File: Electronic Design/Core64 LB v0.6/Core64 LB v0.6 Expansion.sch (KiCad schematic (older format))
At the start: 21 parts, among them J14 HEADER_11-PIN_0.1, J5 HEADER_8-PIN_0.1, J6 HEADER_8-PIN_0.1, U5 74HC238, U8 Adafruit_3.2_TFT_1743, X1 SSW-104-22-L-S-VS, X2 Header_9-PIN_0.1, X3 QWIIC, X4 SAO_conn_SFH11-NBPC-D03-ST-BK

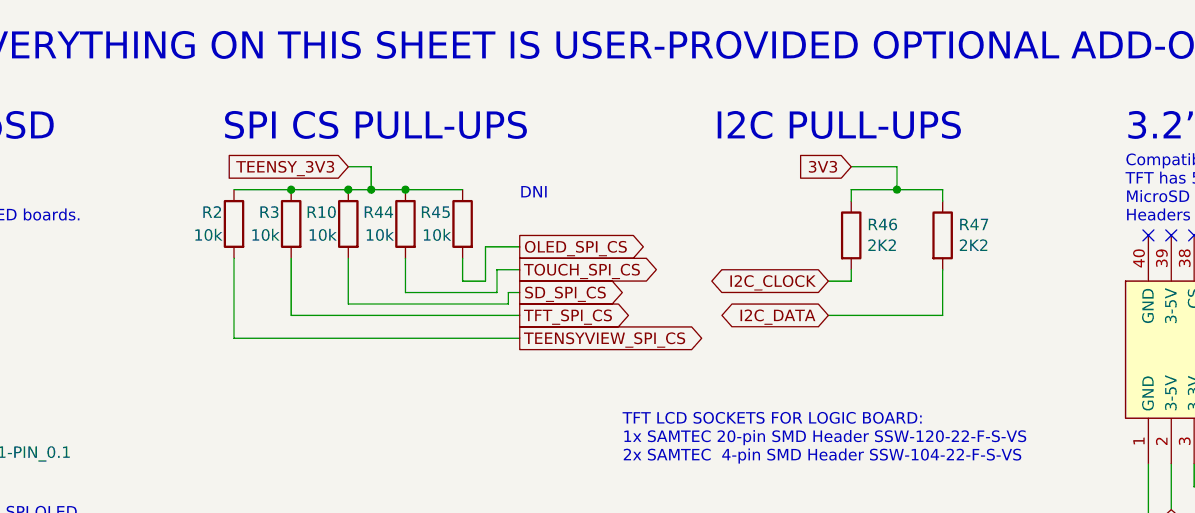
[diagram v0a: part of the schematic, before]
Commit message: APPLY LOGIC BOARD V0.5 FIXES NEEDED TO BE V0.6 U1 silk screen should be placed by pin 1 not pin 7 Check J1 and J2 labels so J1 is on the left, like it is for the Core Board Remove Header for old LED Matrix, since is no longer needed and it is in the way. RTC Notes on schematic, must add THREE things, typo change from TWO. Below JP5 Teensy Charge Enable is a rogue "+" on the silk screen Left of R56 is a dead-end trace stub. Doesn't hurt anything but it's not right. 6.8 Ohm Core Current Limit Resistors can move to 5%. JP1/2 for OLED should be JP1/2 on the OLED silk screen, not JP3/4 Silk screen, left header row, swap SEN1 and SEN2 text so they match to S1 and S2 correctly on the inner perimeter. Move to larger logo and other text on the backside Update silk screen for all boards with P/Ns, bare board. Move top row of TFT LCD support down 0.55mm. Add 470 resistor to gate of core array enable to limit current. Change I2C pull-up resistors from 2.2K to 1.2K 20% (E12 series is most common, and values overlap) Remove two dead-end GND (BAT-) traces between/below Teensy 25/26, and over to QWIIC. Add I2C series resistors 68 Ohm at output of Teensy. Move the 470uF LED 5V0 capacitor, down to be between 5V0 Cur Mon and Teensy Charge enable jumpers, out of the way of the batteries. New stylus position is on left, so the 3V3 capacitor needs to move in a few mm to allow it to pass through. Provide thru-holes for alternate 3.3V and 5V bulk capacitor options. Propagation through sense logic chips was 200ns, reduce PU to 1K2 and remove inline 10Ks. Now 50ns. Voltage divider and other resistors, consolidated to 10K resistors. Keep the two 10K resistors on the 5V0 MON. Add a SJ in series to isolate from Hall Switches. Replace the inline 10K resistors in the all optional Voltage Monitoring lines with closed SJs instead. Clean-up all the horz/vert traces left from removing LED drive header and relocating the driver and 5V0 cap Part substitutions Data sheet updates
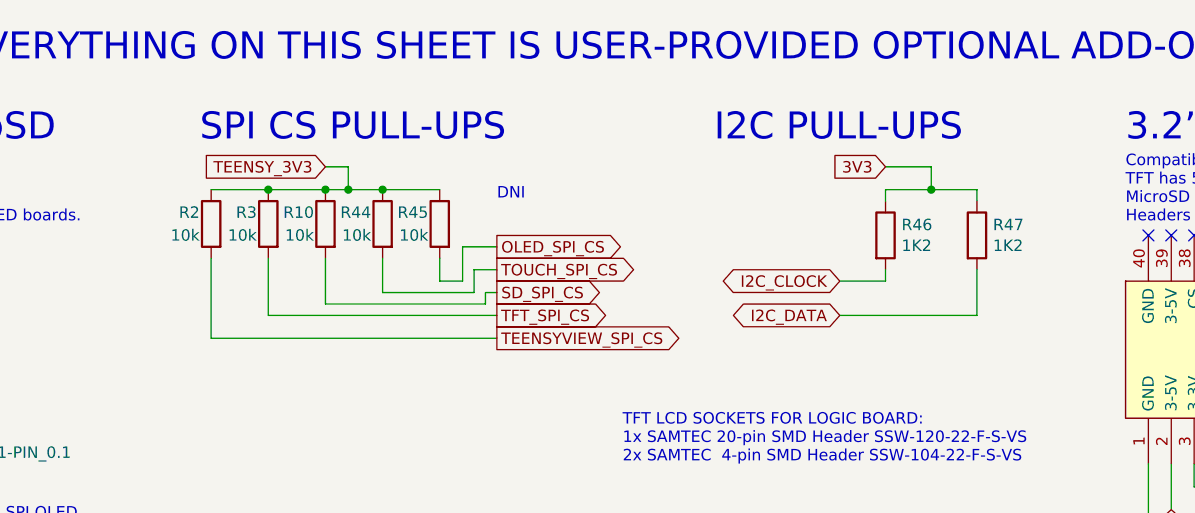
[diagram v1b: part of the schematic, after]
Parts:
- R46, R47: value 2K2 -> 1K2
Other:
- moved on the sheet: R10, R2, R3, R44, R45, R46, R47
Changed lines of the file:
@@
 L Device:R R?
 U 1 1 5FAF4975
-P 6350 1400
+P 6500 1400
 AR Path="/5E755787/5FAF4975" Ref="R?"  Part="1"
 AR Path="/5E755AC8/5D2551FF/5FAF4975" Ref="R?"  Part="1"
 AR Path="/5FAF4975" Ref="R?"  Part="1"
 AR Path="/5EA63449/5FAF4975" Ref="R46"  Part="1"
-F 0 "R46" H 6420 1446 50  0000 L CNN
-F 1 "2K2" H 6420 1355 50  0000 L CNN
-F 2 "Resistor_SMD:R_0805_2012Metric" V 6280 1400 50  0001 C CNN
-F 3 "~" H 6350 1400 50  0001 C CNN
-	1    6350 1400
+F 0 "R46" H 6570 1446 50  0000 L CNN
+F 1 "1K2" H 6570 1355 50  0000 L CNN
+F 2 "Resistor_SMD:R_0805_2012Metric" V 6430 1400 50  0001 C CNN
+F 3 "~" H 6500 1400 50  0001 C CNN
+	1    6500 1400
 	1    0    0    -1
 $EndComp
@@
 L Device:R R?
 U 1 1 5FAF497B
-P 6750 1400
+P 6900 1400
 AR Path="/5E755787/5FAF497B" Ref="R?"  Part="1"
 AR Path="/5E755AC8/5D2551FF/5FAF497B" Ref="R?"  Part="1"
 AR Path="/5FAF497B" Ref="R?"  Part="1"
 AR Path="/5EA63449/5FAF497B" Ref="R47"  Part="1"
-F 0 "R47" H 6820 1446 50  0000 L CNN
-F 1 "2K2" H 6820 1355 50  0000 L CNN
-F 2 "Resistor_SMD:R_0805_2012Metric" V 6680 1400 50  0001 C CNN
-F 3 "~" H 6750 1400 50  0001 C CNN
-	1    6750 1400
-	1    0    0    -1
-$EndComp
-Wire Wire Line
-	6250 1600 6350 1600
-Wire Wire Line
-	6350 1550 6350 1600
-Text GLabel 6250 1750 0    50   BiDi ~ 0
+F 0 "R47" H 6970 1446 50  0000 L CNN
+F 1 "1K2" H 6970 1355 50  0000 L CNN
+F 2 "Resistor_SMD:R_0805_2012Metric" V 6830 1400 50  0001 C CNN
+F 3 "~" H 6900 1400 50  0001 C CNN
+	1    6900 1400
+	1    0    0    -1
+$EndComp
+Wire Wire Line
+	6500 1550 6500 1600
+Text GLabel 6300 1750 0    50   BiDi ~ 0
 I2C_DATA
-Text GLabel 6250 1600 0    50   BiDi ~ 0
+Text GLabel 6300 1600 0    50   BiDi ~ 0
 I2C_CLOCK
 Text Notes 5750 1000 0    118  ~ 0
 I2C PULL-UPS
-Text GLabel 6350 1100 0    50   Input ~ 0
+Text GLabel 6500 1100 0    50   Input ~ 0
 3V3
 Wire Wire Line
-	6750 1200 6750 1250
-Wire Wire Line
-	6550 1100 6350 1100
-Wire Wire Line
-	6350 1200 6350 1250
-Wire Wire Line
-	6350 1200 6550 1200
-Connection ~ 6550 1200
-Wire Wire Line
-	6550 1200 6750 1200
+	6900 1200 6900 1250
+Wire Wire Line
+	6700 1100 6500 1100
+Wire Wire Line
+	6500 1200 6500 1250
+Wire Wire Line
+	6500 1200 6700 1200
+Connection ~ 6700 1200
+Wire Wire Line
+	6700 1200 6900 1200
 $Comp
 L Device:R R?
 U 1 1 5FB255AB
-P 3900 1350
+P 3800 1350
 AR Path="/5E755787/5FB255AB" Ref="R?"  Part="1"
 AR Path="/5E755AC8/5D2551FF/5FB255AB" Ref="R?"  Part="1"
 AR Path="/5FB255AB" Ref="R?"  Part="1"
 AR Path="/5EA63449/5FB255AB" Ref="R3"  Part="1"
-F 0 "R3" H 3950 1400 50  0000 L CNN
-F 1 "10k" H 3950 1300 50  0000 L CNN
-F 2 "Resistor_SMD:R_0805_2012Metric" V 3830 1350 50  0001 C CNN
-F 3 "~" H 3900 1350 50  0001 C CNN
-	1    3900 1350
-	-1   0    0    -1
-$EndComp
-Text GLabel 4900 1750 2    50   Output ~ 0
+F 0 "R3" H 3850 1400 50  0000 L CNN
+F 1 "10k" H 3850 1300 50  0000 L CNN
+F 2 "Resistor_SMD:R_0805_2012Metric" V 3730 1350 50  0001 C CNN
+F 3 "~" H 3800 1350 50  0001 C CNN
+	1    3800 1350
+	-1   0    0    -1
+$EndComp
+Text GLabel 4800 1750 2    50   Output ~ 0
 TFT_SPI_CS
-Text GLabel 4900 1550 2    50   Output ~ 0
+Text GLabel 4800 1550 2    50   Output ~ 0
 TOUCH_SPI_CS
-Text GLabel 4900 1450 2    50   Output ~ 0
+Text GLabel 4800 1450 2    50   Output ~ 0
 OLED_SPI_CS
-Text GLabel 4900 1650 2    50   Output ~ 0
+Text GLabel 4800 1650 2    50   Output ~ 0
 SD_SPI_CS
-Text GLabel 4900 1850 2    50   Output ~ 0
+Text GLabel 4800 1850 2    50   Output ~ 0
 TEENSYVIEW_SPI_CS
 $Comp
 L Device:R R?
 U 1 1 5FB255B6
-P 4150 1350
+P 4050 1350
 AR Path="/5E755787/5FB255B6" Ref="R?"  Part="1"
 AR Path="/5E755AC8/5D2551FF/5FB255B6" Ref="R?"  Part="1"
 AR Path="/5FB255B6" Ref="R?"  Part="1"
 AR Path="/5EA63449/5FB255B6" Ref="R10"  Part="1"
-F 0 "R10" H 4200 1400 50  0000 L CNN
-F 1 "10k" H 4200 1300 50  0000 L CNN
-F 2 "Resistor_SMD:R_0805_2012Metric" V 4080 1350 50  0001 C CNN
-F 3 "~" H 4150 1350 50  0001 C CNN
-	1    4150 1350
+F 0 "R10" H 4100 1400 50  0000 L CNN
+F 1 "10k" H 4100 1300 50  0000 L CNN
+F 2 "Resistor_SMD:R_0805_2012Metric" V 3980 1350 50  0001 C CNN
+F 3 "~" H 4050 1350 50  0001 C CNN
+	1    4050 1350
 	-1   0    0    -1
 $EndComp
@@
 L Device:R R?
 U 1 1 5FB255BC
-P 4400 1350
+P 4300 1350
 AR Path="/5E755787/5FB255BC" Ref="R?"  Part="1"
 AR Path="/5E755AC8/5D2551FF/5FB255BC" Ref="R?"  Part="1"
 AR Path="/5FB255BC" Ref="R?"  Part="1"
 AR Path="/5EA63449/5FB255BC" Ref="R44"  Part="1"
-F 0 "R44" H 4450 1400 50  0000 L CNN
-F 1 "10k" H 4450 1300 50  0000 L CNN
-F 2 "Resistor_SMD:R_0805_2012Metric" V 4330 1350 50  0001 C CNN
-F 3 "~" H 4400 1350 50  0001 C CNN
-	1    4400 1350
+F 0 "R44" H 4350 1400 50  0000 L CNN
+F 1 "10k" H 4350 1300 50  0000 L CNN
+F 2 "Resistor_SMD:R_0805_2012Metric" V 4230 1350 50  0001 C CNN
+F 3 "~" H 4300 1350 50  0001 C CNN
+	1    4300 1350
 	-1   0    0    -1
 $EndComp
@@
 L Device:R R?
 U 1 1 5FB255C2
-P 4650 1350
+P 4550 1350
 AR Path="/5E755787/5FB255C2" Ref="R?"  Part="1"
 AR Path="/5E755AC8/5D2551FF/5FB255C2" Ref="R?"  Part="1"
 AR Path="/5FB255C2" Ref="R?"  Part="1"
 AR Path="/5EA63449/5FB255C2" Ref="R45"  Part="1"
-F 0 "R45" H 4700 1400 50  0000 L CNN
-F 1 "10k" H 4700 1300 50  0000 L CNN
-F 2 "Resistor_SMD:R_0805_2012Metric" V 4580 1350 50  0001 C CNN
-F 3 "~" H 4650 1350 50  0001 C CNN
-	1    4650 1350
+F 0 "R45" H 4600 1400 50  0000 L CNN
+F 1 "10k" H 4600 1300 50  0000 L CNN
+F 2 "Resistor_SMD:R_0805_2012Metric" V 4480 1350 50  0001 C CNN
+F 3 "~" H 4550 1350 50  0001 C CNN
+	1    4550 1350
 	-1   0    0    -1
 $EndComp
@@
 L Device:R R?
 U 1 1 5FB255C8
-P 3650 1350
+P 3550 1350
 AR Path="/5E755787/5FB255C8" Ref="R?"  Part="1"
 AR Path="/5E755AC8/5D2551FF/5FB255C8" Ref="R?"  Part="1"
 AR Path="/5FB255C8" Ref="R?"  Part="1"
 AR Path="/5EA63449/5FB255C8" Ref="R2"  Part="1"
-F 0 "R2" H 3700 1400 50  0000 L CNN
-F 1 "10k" H 3700 1300 50  0000 L CNN
-F 2 "Resistor_SMD:R_0805_2012Metric" V 3580 1350 50  0001 C CNN
-F 3 "~" H 3650 1350 50  0001 C CNN
-	1    3650 1350
-	-1   0    0    -1
-$EndComp
-Wire Wire Line
-	4900 1450 4750 1450
-Wire Wire Line
-	4750 1450 4750 1600
-Wire Wire Line
-	4750 1600 4650 1600
-Wire Wire Line
-	4650 1600 4650 1500
-Wire Wire Line
-	4900 1550 4800 1550
-Wire Wire Line
-	4800 1550 4800 1650
-Wire Wire Line
-	4800 1650 4400 1650
-Wire Wire Line
-	4400 1650 4400 1500
-Wire Wire Line
-	4900 1650 4850 1650
-Wire Wire Line
-	4850 1650 4850 1700
-Wire Wire Line
-	4850 1700 4150 1700
-Wire Wire Line
-	4150 1700 4150 1500
-Wire Wire Line
-	4900 1750 3900 1750
-Wire Wire Line
-	3900 1750 3900 1500
-Wire Wire Line
-	4900 1850 3650 1850
-Wire Wire Line
-	3650 1850 3650 1500
-Connection ~ 3900 1200
-Wire Wire Line
-	3900 1200 3650 1200
+F 0 "R2" H 3600 1400 50  0000 L CNN
+F 1 "10k" H 3600 1300 50  0000 L CNN
+F 2 "Resistor_SMD:R_0805_2012Metric" V 3480 1350 50  0001 C CNN
+F 3 "~" H 3550 1350 50  0001 C CNN
+	1    3550 1350
+	-1   0    0    -1
+$EndComp
+Wire Wire Line
+	4800 1450 4650 1450
+Wire Wire Line
+	4650 1450 4650 1600
+Wire Wire Line
+	4650 1600 4550 1600
+Wire Wire Line
+	4550 1600 4550 1500
+Wire Wire Line
+	4800 1550 4700 1550
+Wire Wire Line
+	4700 1550 4700 1650
+Wire Wire Line
+	4700 1650 4300 1650
+Wire Wire Line
+	4300 1650 4300 1500
+Wire Wire Line
+	4800 1650 4750 1650
+Wire Wire Line
+	4750 1650 4750 1700
+Wire Wire Line
+	4750 1700 4050 1700
+Wire Wire Line
+	4050 1700 4050 1500
+Wire Wire Line
+	4800 1750 3800 1750
+Wire Wire Line
+	3800 1750 3800 1500
+Wire Wire Line
+	4800 1850 3550 1850
+Wire Wire Line
+	3550 1850 3550 1500
+Connection ~ 3800 1200
+Wire Wire Line
+	3800 1200 3550 1200
+Connection ~ 4050 1200
+Wire Wire Line
+	4050 1200 4150 1200
+Connection ~ 4300 1200
+Wire Wire Line
+	4300 1200 4150 1200
+Wire Wire Line
+	4550 1200 4300 1200
+Wire Wire Line
+	4050 1100 4150 1100
 Connection ~ 4150 1200
 Wire Wire Line
-	4150 1200 4250 1200
-Connection ~ 4400 1200
-Wire Wire Line
-	4400 1200 4250 1200
-Wire Wire Line
-	4650 1200 4400 1200
-Wire Wire Line
-	4150 1100 4250 1100
-Connection ~ 4250 1200
-Wire Wire Line
-	4150 1200 3900 1200
-Wire Wire Line
-	4250 1100 4250 1200
-Text Notes 3600 1000 0    118  ~ 0
+	4050 1200 3800 1200
+Wire Wire Line
+	4150 1100 4150 1200
+Text Notes 3500 1000 0    118  ~ 0
 SPI CS PULL-UPS
 Wire Wire Line
-	6550 1100 6550 1200
-Wire Wire Line
-	6750 1550 6750 1750
-Wire Wire Line
-	6750 1750 6250 1750
-Text Notes 4900 1250 0    50   ~ 0
+	6700 1100 6700 1200
+Wire Wire Line
+	6900 1550 6900 1750
+Text Notes 4800 1250 0    50   ~ 0
 DNI
 Text GLabel 6850 3700 0    50   Output ~ 0
@@
 Text Notes 9450 4750 0    59   ~ 0
 CARD DETECT\nDAT2\nD1\nCS (or D3)\nSI (or CMD)\nSO (or D0)\nCLK\nGND\n3V
-Text GLabel 4150 1100 0    50   Input ~ 0
+Text GLabel 4050 1100 0    50   Input ~ 0
 TEENSY_3V3
 $Comp
@@
 Text Notes 650  4500 0    50   ~ 0
 OLED SOCKET FOR LOGIC BOARD:\nSAMTEC 4-pin SMD Header SSW-104-22-F-S-VS
+Wire Wire Line
+	6300 1600 6500 1600
+Wire Wire Line
+	6300 1750 6900 1750
 $EndSCHEMATC

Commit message: Revise LB V0.6, part substitutions, data sheet updates, clean up Ref. Des. to be in order and easier to find on the board in groups
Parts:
- C12: renamed from C10; Description (none) -> CAP; Insert? (none) -> Yes
- JP1, JP2, JP3, JP4: Insert? (none) -> No
- R50: renamed from R2; Description (none) -> RES 10K OHM; Insert? (none) -> No; Value_Modifier (none) -> 20%
- R51: renamed from R3; Description (none) -> RES 10K OHM; Insert? (none) -> No; Value_Modifier (none) -> 20%
- R52: renamed from R10; Description (none) -> RES 10K OHM; Insert? (none) -> No; Value_Modifier (none) -> 20%
- R53: renamed from R44; Description (none) -> RES 10K OHM; Insert? (none) -> No; Value_Modifier (none) -> 20%
- R54: renamed from R45; Description (none) -> RES 10K OHM; Insert? (none) -> No; Value_Modifier (none) -> 20%
- R55: renamed from R46; Description (none) -> RES 1.2K OHM; Insert? (none) -> Yes; Value_Modifier (none) -> 10%
- R56: renamed from R47; Description (none) -> RES 1.2K OHM; Insert? (none) -> Yes; Value_Modifier (none) -> 10%
- X10: renamed from U5; Description (none) -> 3-TO-8 DECODER; Insert? (none) -> No
- X2: renamed from J14; Insert? (none) -> No
- X3: renamed from U8; Description https://www.adafruit.com/product/1743 -> TFT LCD 3.2\" Module; Insert? (none) -> No; MPN (none) -> https://www.adafruit.com/product/1743
- X4: renamed from J5; Insert? (none) -> No
- X5: renamed from J6; Insert? (none) -> No
- X6: renamed from X2; Insert? (none) -> No
- X7: renamed from X1; Insert? (none) -> No
- X8: renamed from X3; Description (none) -> CONN HEADER SMD R/A 4POS 1MM; Insert? (none) -> Yes; MPN (none) -> SM04B-SRSS-TB(LF)(SN); Manufacturer_Name (none) -> JST
- X9: renamed from X4; Description (none) -> CONN HDR 6POS KEYED SOCKET 0.1 T.H.; Insert? (none) -> Yes; MPN (none) -> SFH11-NBPC-D03-ST-BK; Manufacturer_Name (none) -> Sullins
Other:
- note added: "0x29 (47)\n0x30 (48)\n0x31 (49)\n0x32 (50)\n0x33 (51)\n0x57 (87)"
- note added: "0x38 (56)\n0x3C (60)\n0x20 (32)\n0x50 (80)\n0x50-53"
- note added: "AMBIENT PROX. SENSOR\nOLED\nAND!XOR IO Exp. MCP23017\nAND!XOR EEPROM AT24C32r\nNFC CLICK PN7120\n"
- note removed: "0X29 (47)\n0x30 (48)\n0x31 (49)\n0x32 (50)\n0x33 (51)\n0x57 (87)"
- note removed: "0x3C (60)\n0x20 (32)\n0x50 (80)\n0x50-53\n0x50 (N.C.)"
- note removed: "OLED\nAND!XOR IO Exp. MCP23017\nAND!XOR EEPROM AT24C32r\nNFC CLICK PN7120\nPIMORONI UNICORN HAT"

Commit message: Refine LB v0.6 layout, KiCAD BOM updates, review schematic and PCB for release
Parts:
- C12: Insert? Yes -> No
- renumbered JP1 to JP15, JP2 to JP16, JP3 to JP17, JP4 to JP18, X10 to U8
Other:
- note added: "To use more than 1 core plane (not compatible with Hall Switches):\n1) Add 3-to-8 decoder 74HC238 and decoupling capacitor.\n2) Cut both SJ pads (1-2) and close pads (2-3) for CP1 and 2_EN.\n3) Cut SJs 1-4 on DRIVER Sheet for CP5-8 if Hall Switches installed.\nNOTES:\nSee Core Board schematic for other required CB changes.\nSAO#1 (LB) GPIO is still accessible as CP_ADDR_0 and 1, shared.\nSAO#2 (C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"
- note removed: "To use more than 1 core plane:\n1) Add 3-to-8 decoder 74HC238 and decoupling capacitor.\n2) Cut both SJ pads 1-2 and solder pads 2-3.\n3) Cut 4 SJs 9-12 on DRIVER Sheet near left 20p socket for CP5-8.\nNOTES:\nSee Core Board schematic for other required CB changes.\nSAO#1 (LB) GPIO is still accessible as CP_ADDR_0 and 1, shared.\nSAO#2 (CB) GPIO becomes output [only] Y0 and Y1 of CP selector.\nSP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"
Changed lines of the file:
@@
 Sheet 3 5
 Title "Core 64 - Expansion"
-Date "2021-11-08"
+Date "2021-11-09"
 Rev "0.6"
 Comp "Concept and design by Andy Geppert @ www.MachineIdeas.com"
 Comment1 "Visit www.Core64.io for information on assembly and optional features."
-Comment2 "WIP"
+Comment2 "As released"
 Comment3 ""
 Comment4 "All non-polarized capacitors are X7R or X5R ceramic unless otherwise noted."
@@
 	5900 5800 5900 5650
 $Comp
-L Jumper:SolderJumper_3_Open JP2
+L Jumper:SolderJumper_3_Open JP16
 U 1 1 5E81A96A
 P 1750 5600
-F 0 "JP2" V 1600 5650 50  0000 L CNN
+F 0 "JP16" V 1600 5650 50  0000 L CNN
 F 1 "SolderJumper_3_Open" V 1350 5150 50  0001 L CNN
 F 2 "Jumper:SolderJumper-3_P1.3mm_Open_Pad1.0x1.5mm_NumberLabels" H 1750 5600 50  0001 C CNN
@@
 	8750 4600 9150 4600
 $Comp
-L Jumper:SolderJumper_3_Open JP1
+L Jumper:SolderJumper_3_Open JP15
 U 1 1 5E82F3CE
 P 1450 5500
-F 0 "JP1" V 1550 5550 50  0000 L CNN
+F 0 "JP15" V 1550 5550 50  0000 L CNN
 F 1 "SolderJumper_3_Open" V 800 5400 50  0001 L CNN
 F 2 "Jumper:SolderJumper-3_P1.3mm_Open_Pad1.0x1.5mm_NumberLabels" H 1450 5500 50  0001 C CNN
@@
 F 2 "Capacitor_SMD:C_0805_2012Metric" H 1688 6750 50  0001 C CNN
 F 3 "~" H 1650 6900 50  0001 C CNN
-F 4 "Yes" H 1650 6900 50  0001 C CNN "Insert?"
+F 4 "No" H 1650 6900 50  0001 C CNN "Insert?"
 F 5 "CAP" H 1650 6900 50  0001 C CNN "Description"
 	1    1650 6900
@@
 Connection ~ 2000 6950
 $Comp
-L 74xx_IEEE:74HC238 X10
+L 74xx_IEEE:74HC238 U8
 U 1 1 5F6FED24
 P 2550 7150
-F 0 "X10" H 2800 7650 50  0000 C CNN
+F 0 "U8" H 2800 7650 50  0000 C CNN
 F 1 "74HC238" H 2800 7550 50  0000 C CNN
 F 2 "Digikey:TSSOP-16-W4.40mm" H 2550 7150 50  0001 C CNN
@@
 EVERYTHING ON THIS SHEET IS USER-PROVIDED OPTIONAL ADD-ONS
 Text Notes 3500 8000 0    50   ~ 0
-To use more than 1 core plane:\n1) Add 3-to-8 decoder 74HC238 and decoupling capacitor.\n2) Cut both SJ pads 1-2 and solder pads 2-3.\n3) Cut 4 SJs 9-12 on DRIVER Sheet near left 20p socket for CP5-8.\nNOTES:\nSee Core Board schematic for other required CB changes.\nSAO#1 (LB) GPIO is still accessible as CP_ADDR_0 and 1, shared.\nSAO#2 (CB) GPIO becomes output [only] Y0 and Y1 of CP selector.\nSPARE GPIO 1-2-3 are used for Core Plane Addressing.
+To use more than 1 core plane (not compatible with Hall Switches):\n1) Add 3-to-8 decoder 74HC238 and decoupling capacitor.\n2) Cut both SJ pads (1-2) and close pads (2-3) for CP1 and 2_EN.\n3) Cut SJs 1-4 on DRIVER Sheet for CP5-8 if Hall Switches installed.\nNOTES:\nSee Core Board schematic for other required CB changes.\nSAO#1 (LB) GPIO is still accessible as CP_ADDR_0 and 1, shared.\nSAO#2 (CB) GPIO becomes output [only] Y0 and Y1 of CP selector.\nSPARE GPIO 1-2-3 are used for Core Plane Addressing.
 Wire Wire Line
 	3850 7050 3800 7050
 $Comp
-L Jumper:SolderJumper_3_Bridged12 JP4
+L Jumper:SolderJumper_3_Bridged12 JP18
 U 1 1 5F5AEC4F
 P 3600 7050
-F 0 "JP4" H 3550 7150 50  0000 L CNN
+F 0 "JP18" H 3550 7150 50  0000 L CNN
 F 1 "SolderJumper_3_Open" V 3200 6600 50  0001 L CNN
 F 2 "Jumper:SolderJumper-3_P1.3mm_Bridged12_RoundedPad1.0x1.5mm_NumberLabels" H 3600 7050 50  0001 C CNN
@@
 $EndComp
 $Comp
-L Jumper:SolderJumper_3_Bridged12 JP3
+L Jumper:SolderJumper_3_Bridged12 JP17
 U 1 1 5F5B143C
 P 3600 6700
-F 0 "JP3" H 3550 6800 50  0000 L CNN
+F 0 "JP17" H 3550 6800 50  0000 L CNN
 F 1 "SolderJumper_3_Open" V 3200 6250 50  0001 L CNN
 F 2 "Jumper:SolderJumper-3_P1.3mm_Bridged12_RoundedPad1.0x1.5mm_NumberLabels" H 3600 6700 50  0001 C CNN
